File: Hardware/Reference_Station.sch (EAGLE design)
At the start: 245 parts, among them J10 ANTENNA-SMA-GROUNDEDEDGE_SMA, J11 Vertical Qwiic Connector, J2 ANTENNA-SMA-GROUNDEDEDGE_SMA, J3 MICRO-SD-PUSH-PUSH-EXT-PIN, J4 Vertical Qwiic Connector, J7 ANTENNA-SMA-GROUNDEDEDGE_RPSMA, J9 MAGJACK-POE, U1 ESP-WROOM-32E, U10 POE_PSU-DP990X, U11 OPA344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

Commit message: v10 Hardware
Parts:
- removed VPOE7: TEST-POINTPOGO_PTH, SparkFun-Connectors:TEST-POINTPOGO_PTH
- added C58: 0.1uF, SparkFun-Capacitors:0.1UF-0603-25V-5%
- added DET, GND: TEST-POINTPOGO_PTH, SparkFun-Connectors:TEST-POINTPOGO_PTH
- added GNSS_RESET: JUMPER-COMBO_2_NO, SparkFun-Jumpers:JUMPER-COMBO_2_NO
- added R64: 10k, SparkFun-Resistors:10KOHM-0603-1/10W-1%
- added R65: 100k, SparkFun-Resistors:100KOHM-0603-1/10W-1%
- C31: value DNP -> 0.1uF; device SparkFun-Capacitors:DNP-0603_NO_CREAM -> SparkFun-Capacitors:0.1UF-0603-25V-5%
- U8: value ADC8045 -> MCP6021T; device SparkFun-IC-Amplifiers:AD8045-PAD -> SparkFun-IC-Amplifiers:MCP6021T-E/OT
- U9: value 74HC4066_QUAD_BILATERAL_SWITCH_QFN -> 74LVC4066D_QUAD_BILATERAL_SWITCH; device SparkFun-IC-Logic:74HC4066_QUAD_BILATERAL_SWITCH_QFN -> SparkFun-IC-Logic:74LVC4066D_QUAD_BILATERAL_SWITCH
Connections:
- removed net N$16: R9.2, U8.OUT
- new net DET: DET.1, J3.DET, R65.1, U1.SENSOR_VP/IA36
- new net GNSS_!RESET!: C58.1, GNSS_RESET.1, R64.1, U4.!RESET!
- net !RESET!: now also GNSS_RESET.2; no longer U4.!RESET!
- net 3.3V: now also R64.2
- net 3.3V_SW: now also R65.2
- net 5V: now also U8G2.P$V+; no longer U8.+VS
- net ESP25/TP: now also U8G1.+IN; no longer U8.IN+
- net GND: now also C58.2, GND.1, U8G2.P$V-; no longer U8.-VS, U8.PAD, VPOE7.1
- net N$18: now also U8G1.-IN; no longer U8.IN-
- net N$26: now also R9.2, U8G1.OUT; no longer U8.FB
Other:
- note added: "v10"
- note removed: "v01"
- moved on the sheet: C1, C19, C2, C22, C23, J10, J3, R18, R23, R44, R9, U9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

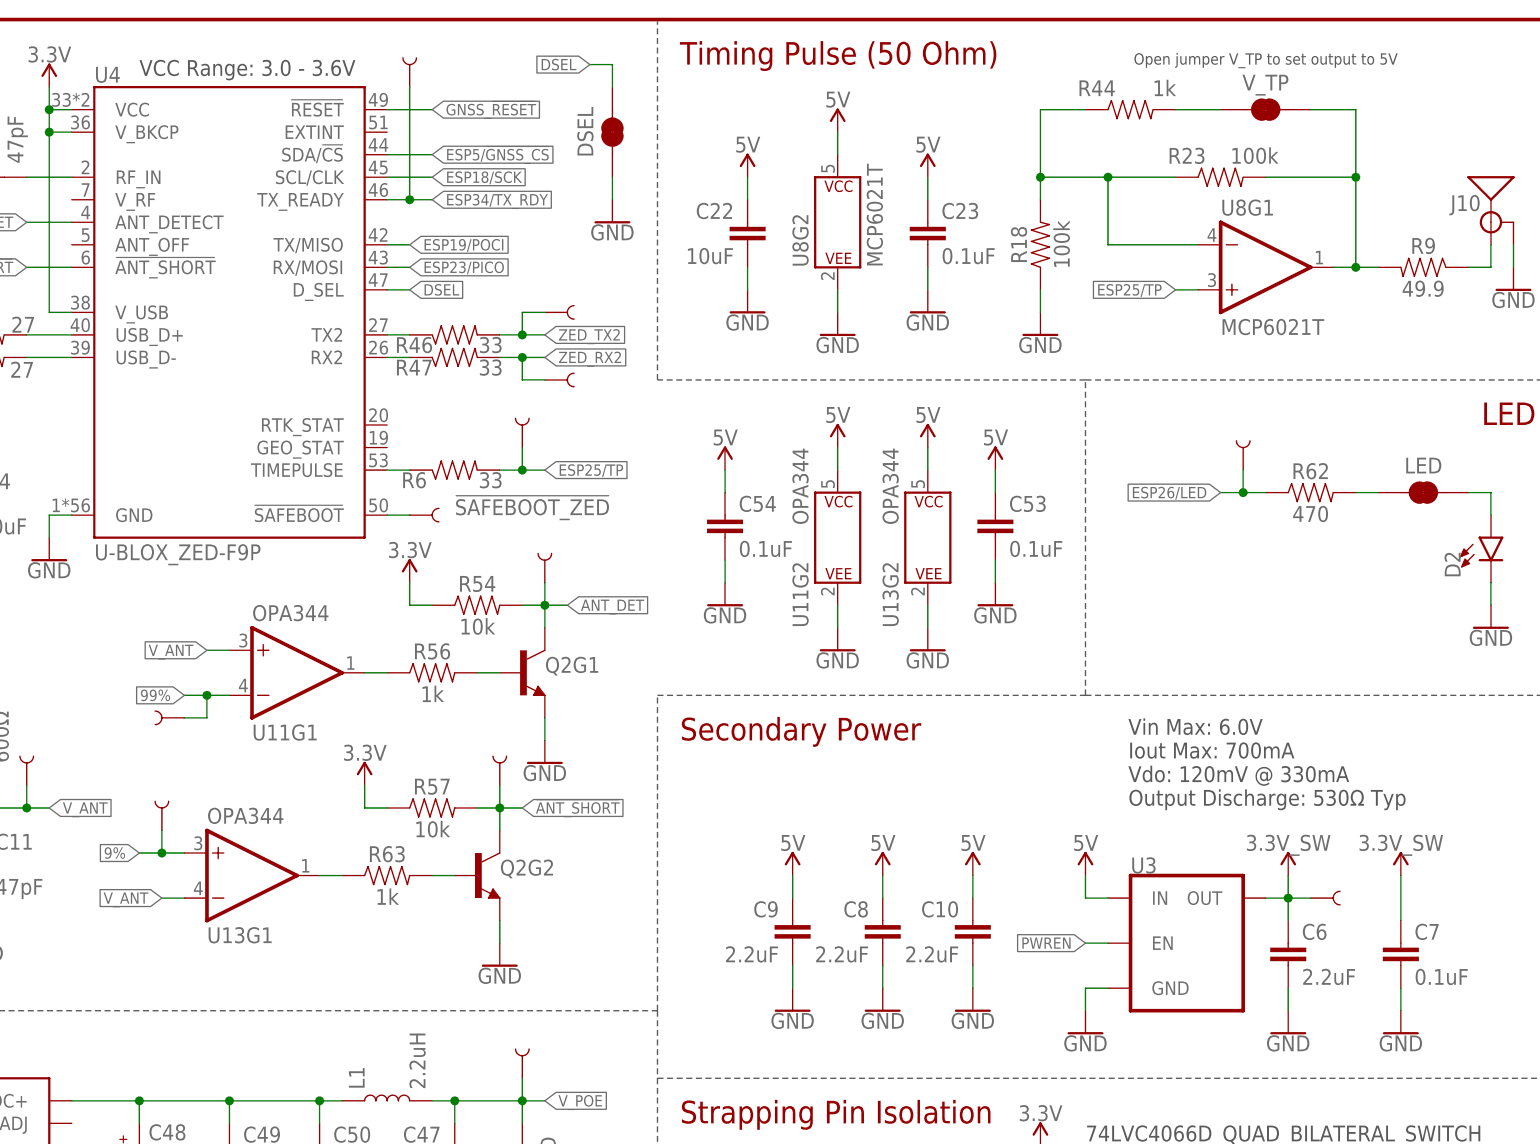
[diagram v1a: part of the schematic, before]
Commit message: Improve TP output at 5V
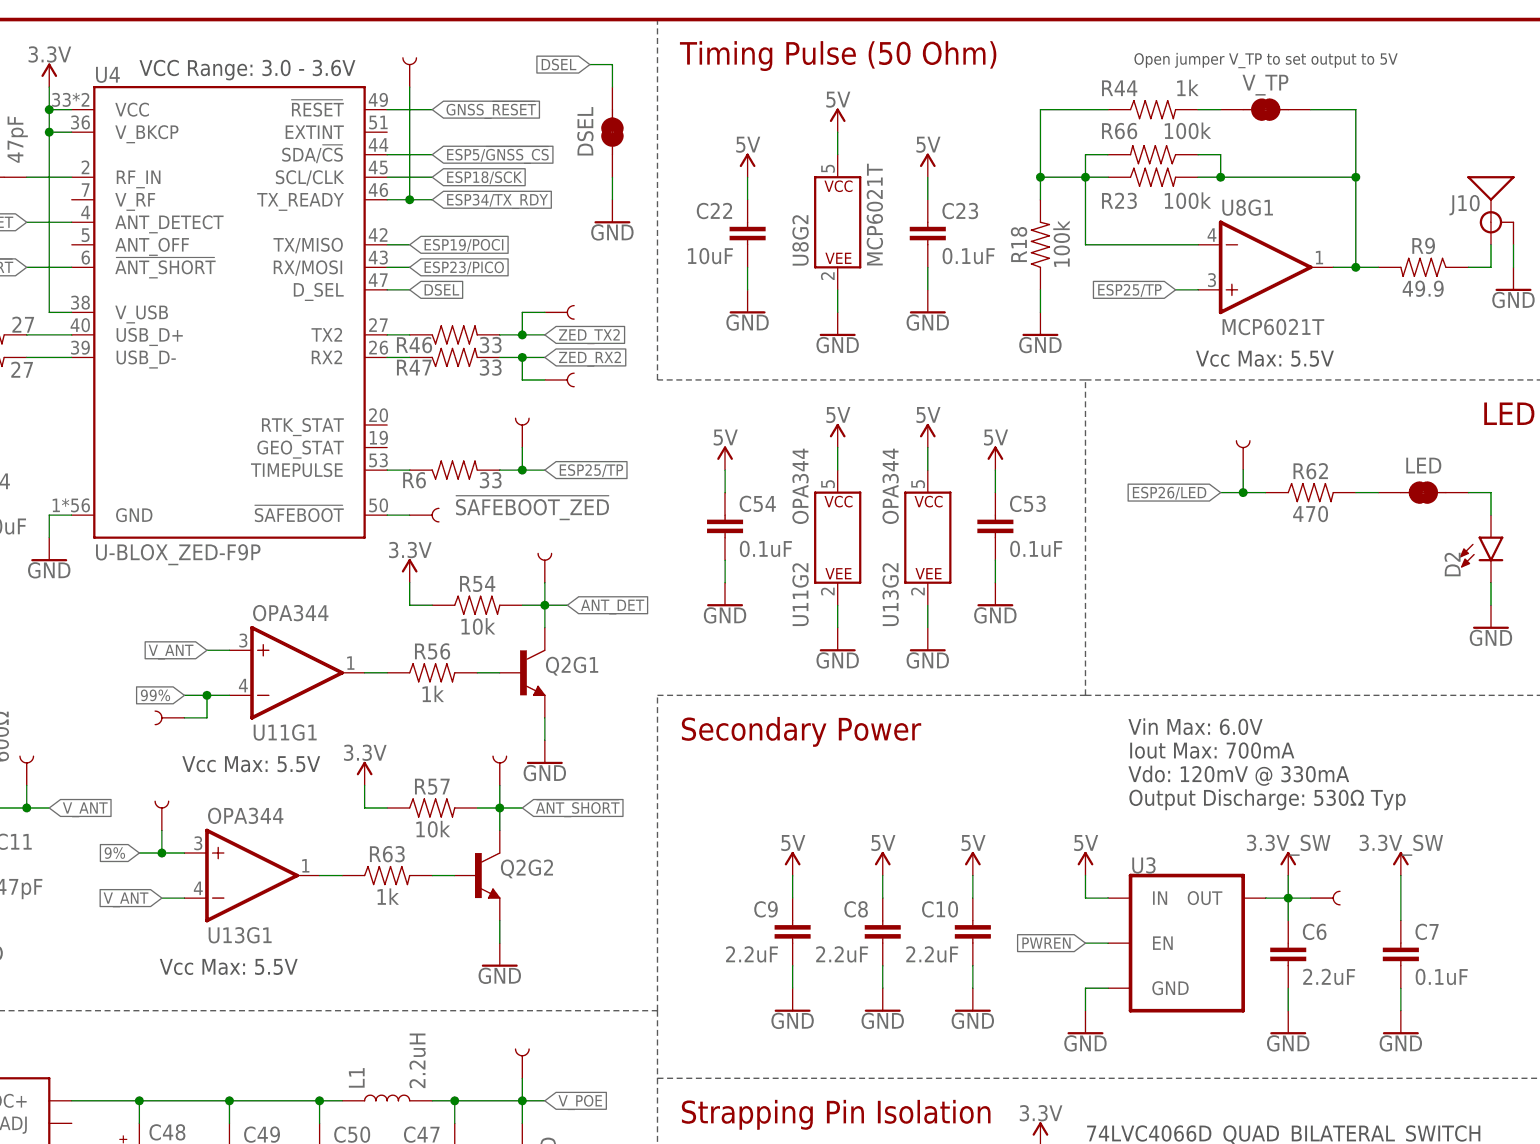
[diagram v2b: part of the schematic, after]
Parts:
- added R66: 100k, SparkFun-Resistors:100KOHM-0603-1/10W-1%
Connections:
- net N$18: now also R66.2
- net N$26: now also R66.1
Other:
- note added: "Vcc Max: 5.5V"
- moved on the sheet: R23, R44
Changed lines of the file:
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@@
 <part name="DET" library="SparkFun-Connectors" deviceset="TEST-POINT" device="POGO_PTH" value="TEST-POINTPOGO_PTH"/>
 <part name="U8" library="SparkFun-IC-Amplifiers" deviceset="MCP6021" device="T-E/OT" value="MCP6021T"/>
+<part name="R66" library="SparkFun-Resistors" deviceset="100KOHM" device="-0603-1/10W-1%" value="100k"/>
 </parts>
 <sheets>
@@
 <text x="215.9" y="40.64" size="2.54" layer="94" font="vector" align="top-right">I/O Connector</text>
 <wire x1="220.98" y1="43.18" x2="220.98" y2="0" width="0.1524" layer="97" style="longdash"/>
+<text x="390.906" y="240.284" size="1.778" layer="97" font="vector">Vcc Max: 5.5V</text>
+<text x="276.606" y="194.564" size="1.778" layer="97" font="vector">Vcc Max: 5.5V</text>
+<text x="274.066" y="171.704" size="1.778" layer="97" font="vector">Vcc Max: 5.5V</text>
 </plain>
 <instances>
@@
 <attribute name="VALUE" x="373.38" y="243.586" size="1.778" layer="96" align="top-center"/>
 </instance>
-<instance part="R23" gate="G$1" x="393.7" y="261.62" smashed="yes">
-<attribute name="NAME" x="389.89" y="263.144" size="1.778" layer="95" font="vector" align="bottom-center"/>
-<attribute name="VALUE" x="397.51" y="263.144" size="1.778" layer="96" font="vector" rot="R180" align="top-center"/>
-</instance>
-<instance part="R44" gate="G$1" x="383.54" y="269.24" smashed="yes">
-<attribute name="NAME" x="379.73" y="270.764" size="1.778" layer="95" font="vector" align="bottom-center"/>
-<attribute name="VALUE" x="387.35" y="270.764" size="1.778" layer="96" font="vector" rot="R180" align="top-center"/>
+<instance part="R23" gate="G$1" x="386.08" y="261.62" smashed="yes">
+<attribute name="NAME" x="382.27" y="258.064" size="1.778" layer="95" font="vector" align="bottom-center"/>
+<attribute name="VALUE" x="389.89" y="258.064" size="1.778" layer="96" font="vector" rot="R180" align="top-center"/>
+</instance>
+<instance part="R44" gate="G$1" x="386.08" y="269.24" smashed="yes">
+<attribute name="NAME" x="382.27" y="270.764" size="1.778" layer="95" font="vector" align="bottom-center"/>
+<attribute name="VALUE" x="389.89" y="270.764" size="1.778" layer="96" font="vector" rot="R180" align="top-center"/>
 </instance>
 <instance part="PW+" gate="JP1" x="233.68" y="157.48" smashed="yes" rot="R180">
@@
 <attribute name="VALUE" x="355.6" y="251.46" size="1.778" layer="95" font="vector" rot="R90"/>
 </instance>
+<instance part="R66" gate="G$1" x="386.08" y="264.16" smashed="yes" rot="R180">
+<attribute name="NAME" x="382.27" y="267.716" size="1.778" layer="95" font="vector" rot="R180" align="bottom-center"/>
+<attribute name="VALUE" x="389.89" y="267.716" size="1.778" layer="96" font="vector" align="top-center"/>
+</instance>
 </instances>
 <busses>
@@
 <net name="N$18" class="0">
 <segment>
-<wire x1="381" y1="261.62" x2="373.38" y2="261.62" width="0.1524" layer="91"/>
+<wire x1="378.46" y1="261.62" x2="373.38" y2="261.62" width="0.1524" layer="91"/>
 <wire x1="373.38" y1="269.24" x2="373.38" y2="261.62" width="0.1524" layer="91"/>
 <pinref part="R18" gate="G$1" pin="2"/>
 <pinref part="R44" gate="G$1" pin="1"/>
-<wire x1="378.46" y1="269.24" x2="373.38" y2="269.24" width="0.1524" layer="91"/>
+<wire x1="381" y1="269.24" x2="373.38" y2="269.24" width="0.1524" layer="91"/>
 <pinref part="R23" gate="G$1" pin="1"/>
 <wire x1="373.38" y1="259.08" x2="373.38" y2="261.62" width="0.1524" layer="91"/>
 <junction x="373.38" y="261.62"/>
 <pinref part="U8" gate="G1" pin="-IN"/>
-<wire x1="391.16" y1="254" x2="381" y2="254" width="0.1524" layer="91"/>
-<wire x1="381" y1="254" x2="381" y2="261.62" width="0.1524" layer="91"/>
-<wire x1="381" y1="261.62" x2="388.62" y2="261.62" width="0.1524" layer="91"/>
-<junction x="381" y="261.62"/>
+<wire x1="391.16" y1="254" x2="378.46" y2="254" width="0.1524" layer="91"/>
+<wire x1="378.46" y1="254" x2="378.46" y2="261.62" width="0.1524" layer="91"/>
+<wire x1="378.46" y1="261.62" x2="381" y2="261.62" width="0.1524" layer="91"/>
+<junction x="378.46" y="261.62"/>
+<pinref part="R66" gate="G$1" pin="2"/>
+<wire x1="381" y1="264.16" x2="378.46" y2="264.16" width="0.1524" layer="91"/>
+<wire x1="378.46" y1="264.16" x2="378.46" y2="261.62" width="0.1524" layer="91"/>
 </segment>
 </net>
@@
 <wire x1="408.94" y1="269.24" x2="408.94" y2="261.62" width="0.1524" layer="91"/>
 <pinref part="R23" gate="G$1" pin="2"/>
-<wire x1="398.78" y1="261.62" x2="408.94" y2="261.62" width="0.1524" layer="91"/>
+<wire x1="391.16" y1="261.62" x2="393.7" y2="261.62" width="0.1524" layer="91"/>
 <pinref part="V_TP" gate="G$1" pin="2"/>
+<wire x1="393.7" y1="261.62" x2="408.94" y2="261.62" width="0.1524" layer="91"/>
 <wire x1="403.86" y1="269.24" x2="408.94" y2="269.24" width="0.1524" layer="91"/>
 <pinref part="U8" gate="G1" pin="OUT"/>
@@
 <junction x="408.94" y="261.62"/>
 <junction x="408.94" y="251.46"/>
+<pinref part="R66" gate="G$1" pin="1"/>
+<wire x1="391.16" y1="264.16" x2="393.7" y2="264.16" width="0.1524" layer="91"/>
+<wire x1="393.7" y1="264.16" x2="393.7" y2="261.62" width="0.1524" layer="91"/>
+<junction x="393.7" y="261.62"/>
 </segment>
 </net>
@@
 <pinref part="R44" gate="G$1" pin="2"/>
 <pinref part="V_TP" gate="G$1" pin="1"/>
-<wire x1="388.62" y1="269.24" x2="393.7" y2="269.24" width="0.1524" layer="91"/>
+<wire x1="391.16" y1="269.24" x2="393.7" y2="269.24" width="0.1524" layer="91"/>
 </segment>
 </net>

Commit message: Replace OPA344 with MCP6021T-E/OT
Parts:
- U11, U13: value OPA344 -> MCP6021T; device SparkFun-IC-Amplifiers:OPA344 -> SparkFun-IC-Amplifiers:MCP6021T-E/OT
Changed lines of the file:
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@@
 <setting verticaltext="up"/>
 </settings>
-<grid distance="0.1" unitdist="inch" unit="inch" style="lines" multiple="1" display="no" altdistance="0.05" altunitdist="inch" altunit="inch"/>
+<grid distance="0.1" unitdist="inch" unit="inch" style="lines" multiple="1" display="no" altdistance="0.01" altunitdist="inch" altunit="inch"/>
 <layers>
 <layer number="1" name="Top" color="4" fill="1" visible="no" active="no"/>
@@
 <part name="R46" library="SparkFun-Resistors" deviceset="33OHM" device="-0603-1/10W-1%" value="33"/>
 <part name="R47" library="SparkFun-Resistors" deviceset="33OHM" device="-0603-1/10W-1%" value="33"/>
-<part name="U11" library="SparkFun-IC-Amplifiers" deviceset="OPA344" device="" value="OPA344"/>
+<part name="U11" library="SparkFun-IC-Amplifiers" deviceset="MCP6021" device="T-E/OT" value="MCP6021T"/>
 <part name="C54" library="SparkFun-Capacitors" deviceset="0.1UF" device="-0603-25V-5%" value="0.1uF"/>
 <part name="GND93" library="SparkFun-PowerSymbols" deviceset="GND" device=""/>
@@
 <part name="SUPPLY60" library="SparkFun-PowerSymbols" deviceset="3.3V" device=""/>
 <part name="R56" library="SparkFun-Resistors" deviceset="1KOHM" device="-0603-1/10W-1%" value="1k"/>
-<part name="U13" library="SparkFun-IC-Amplifiers" deviceset="OPA344" device="" value="OPA344"/>
+<part name="U13" library="SparkFun-IC-Amplifiers" deviceset="MCP6021" device="T-E/OT" value="MCP6021T"/>
 <part name="GND92" library="SparkFun-PowerSymbols" deviceset="GND" device=""/>
 <part name="SUPPLY62" library="SparkFun-PowerSymbols" deviceset="5V" device=""/>

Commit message: Change LED to GREEN
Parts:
- D2: value LED-RIGHT-ANGLE-PTH-BLUE -> LED-RIGHT-ANGLE-PTH-GREEN; device SparkFun-LED:LED-RIGHT-ANGLE-PTH-BLUE -> SparkFun-LED:LED-RIGHT-ANGLE-PTH-GREEN
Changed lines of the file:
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@@
 <setting verticaltext="up"/>
 </settings>
-<grid distance="0.1" unitdist="inch" unit="inch" style="lines" multiple="1" display="no" altdistance="0.01" altunitdist="inch" altunit="inch"/>
+<grid distance="0.1" unitdist="inch" unit="inch" style="lines" multiple="1" display="no" altdistance="0.05" altunitdist="inch" altunit="inch"/>
 <layers>
 <layer number="1" name="Top" color="4" fill="1" visible="no" active="no"/>
@@
 <part name="BOOT" library="SparkFun-Switches" deviceset="MOMENTARY-SWITCH-SPST" device="-PTH-RIGHT-ANGLE-8-020" value="MOMENTARY-SWITCH-SPST-PTH-RIGHT-ANGLE-8-020"/>
 <part name="LED" library="SparkFun-Jumpers" deviceset="JUMPER-SMT_2_NC_TRACE" device="_SILK" package3d_urn="urn:adsk.eagle:package:39281/1" value="JUMPER-SMT_2_NC_TRACE_SILK"/>
-<part name="D2" library="SparkFun-LED" deviceset="LED-RIGHT-ANGLE-PTH" device="-BLUE"/>
+<part name="D2" library="SparkFun-LED" deviceset="LED-RIGHT-ANGLE-PTH" device="-GREEN" value="LED-RIGHT-ANGLE-PTH-GREEN"/>
 <part name="R62" library="SparkFun-Resistors" deviceset="470OHM" device="-0603-1/10W-1%" value="470"/>
 <part name="C5" library="SparkFun-Capacitors" deviceset="2.2UF" device="-0603-10V-20%" value="2.2uF"/>
